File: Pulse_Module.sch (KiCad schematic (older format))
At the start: 0 parts

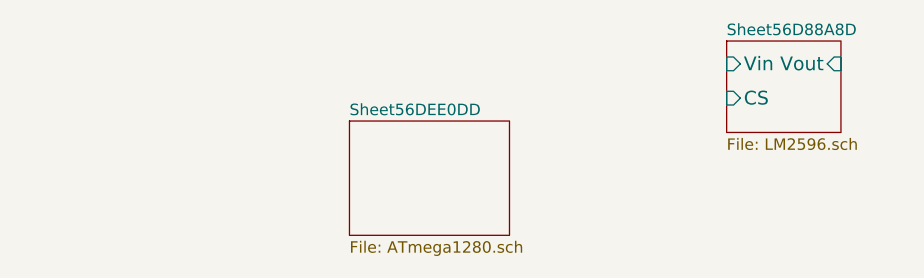
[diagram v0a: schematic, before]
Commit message: Добавление 40пинового разъёма и UART
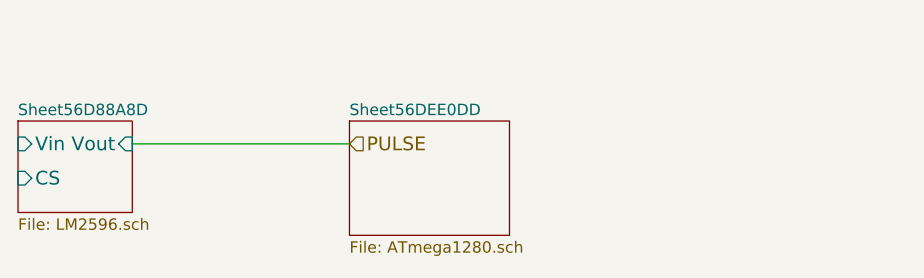
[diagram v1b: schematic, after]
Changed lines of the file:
@@
 EESchema Schematic File Version 2
+LIBS:pl2303
 LIBS:power
 LIBS:device
@@
 $Descr A4 11693 8268
 encoding utf-8
-Sheet 1 3
+Sheet 1 4
 Title ""
-Date "14 mar 2016"
+Date "7 apr 2016"
 Rev ""
 Comp ""
@@
 $EndDescr
 $Sheet
-S 6100 3300 500  400
+S 3000 3650 500  400
 U 56D88A8E
 F0 "Sheet56D88A8D" 50
 F1 "LM2596.sch" 50
-F2 "Vin" I L 6100 3400 60
-F3 "Vout" I R 6600 3400 60
-F4 "CS" I L 6100 3550 60
+F2 "Vin" I L 3000 3750 60
+F3 "Vout" I R 3500 3750 60
+F4 "CS" I L 3000 3900 60
 $EndSheet
 $Sheet
@@
 F1 "ATmega1280.sch" 50
 $EndSheet
+Text HLabel 4450 3750 2    60   Input ~ 0
+PULSE
+Wire Wire Line
+	3500 3750 4450 3750
 $EndSCHEMATC

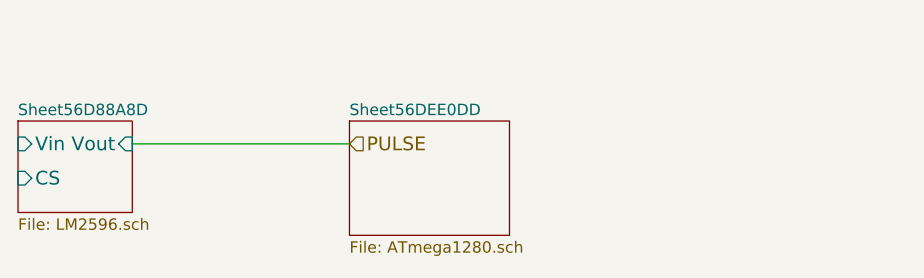
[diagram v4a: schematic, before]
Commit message: Добавление WS2812, исправление всех замечаний
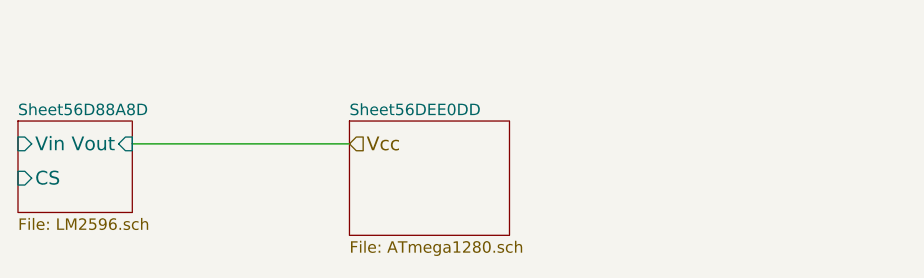
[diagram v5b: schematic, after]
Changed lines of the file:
@@
 EESchema Schematic File Version 2
+LIBS:Pulse_Module-rescue
 LIBS:conn3
 LIBS:pl2303
@@
 LIBS:philips
 LIBS:display
+LIBS:ws2812
 LIBS:cypress
 LIBS:siliconi
@@
 LIBS:valves
 LIBS:Pulse_Module-cache
-EELAYER 27 0
+EELAYER 25 0
 EELAYER END
 $Descr A4 11693 8268
@@
 $EndSheet
 Text HLabel 4450 3750 2    60   Input ~ 0
-PULSE
+Vcc
 Wire Wire Line
 	3500 3750 4450 3750
